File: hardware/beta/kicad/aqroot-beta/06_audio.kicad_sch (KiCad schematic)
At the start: 6 parts, among them U5 MAX98357A

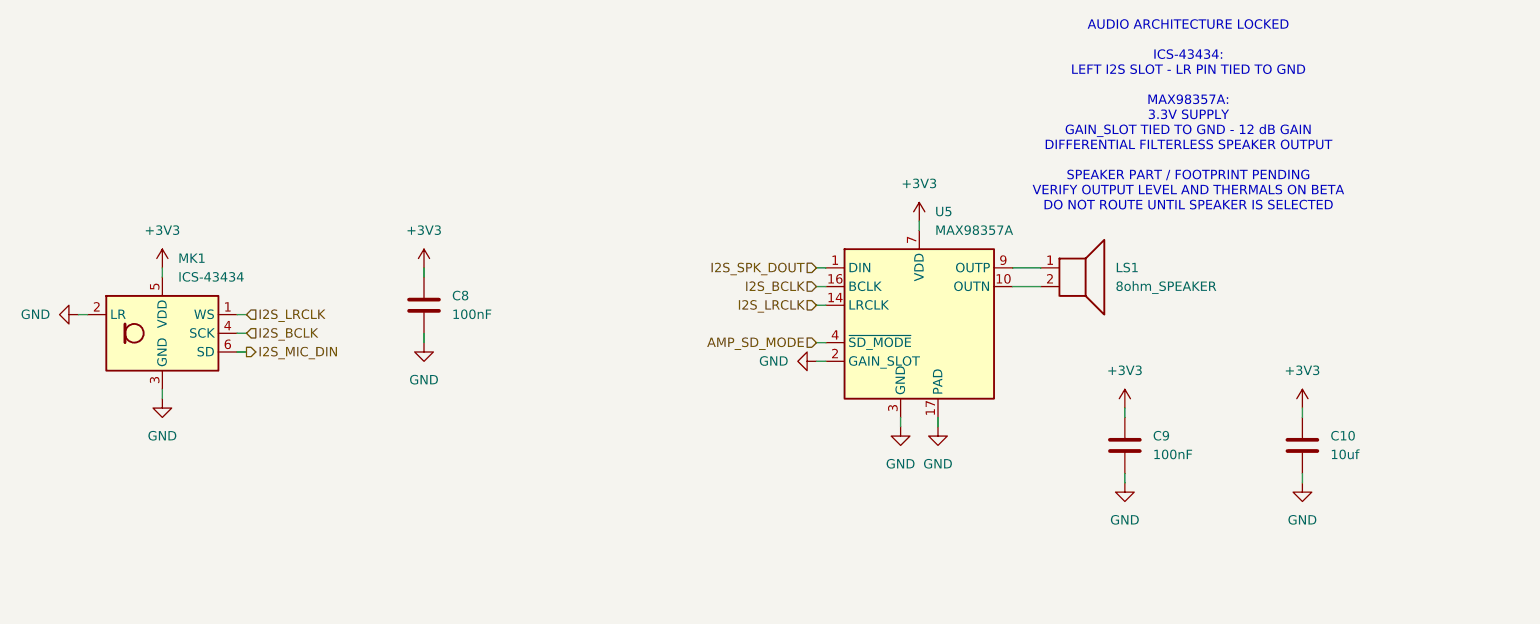
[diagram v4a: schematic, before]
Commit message: AQROOT Beta: convert speaker to off-board JST connection
Implements OPTION C, off-board wired speaker.

LS1 is reclassified OFF_BOARD. Value becomes 8R_SPEAKER_OFFBOARD, Mounting is
OFF_BOARD, and the previously locked board-mounted SKU (Same Sky CMS-1535-058SP)
is retired in favour of a class spec: 8 ohm, >=0.5 W, ~15 mm class, SKU
FINALIZES WITH ENCLOSURE. The symbol is marked exclude-from-board, so LS1 is
intentionally footprintless and drops out of the board netlist. No PCB footprint
was created for the speaker body, by design.

J6 added - JST B2B-PH-K-S, PH series, 2.00 mm pitch, board-side vertical
through-hole header, footprint
Connector_JST:JST_PH_B2B-PH-K_1x02_P2.00mm_Vertical. Verified before assignment:
2 pads, 2.00 mm pitch, through-hole, vertical, pin 1 keyed roundrect and pin 2
oval, drill 0.75, citing JST's own ePH.pdf. This is the same land pattern already
used by the J4 battery connector, so the choice is consistent with existing repo
practice. J6 is the next free connector reference; J1-J5 were not reused.

The MAX98357A path and amplifier architecture are unchanged. The differential
output pair is now named for polarity: U5 OUTP -> SPK_P -> J6 pin 1, U5 OUTN ->
SPK_N -> J6 pin 2, with LS1 shown on the same nodes as the off-board load. A
sheet note records OFF-BOARD SPEAKER / 8R >=0.5W / JST PH 2.0 mm /
ENCLOSURE-MOUNTED plus the pin-to-polarity mapping, and the stale
"DO NOT ROUTE UNTIL SPEAKER IS SELECTED" note is replaced.

Netlist delta is exactly the intended one: J6 joins SPK_P and SPK_N, U5 pins 9
and 10 move from the auto-named Net-(U5-OUTP/OUTN) to the labelled SPK_P/SPK_N,
and LS1 leaves the board netlist because it is now off-board. Net count is
unchanged at 174 - the two auto-named nets were renamed, not added. Nothing else
in the design changed. Canonical ERC holds at 58 raw / 5 errors / 53 warnings
with 58 live exclusions, 0 stale and 0 unexplained real defects.

Board-mounted missing footprints are now SW1-SW8 only.

Co-Authored-By: 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
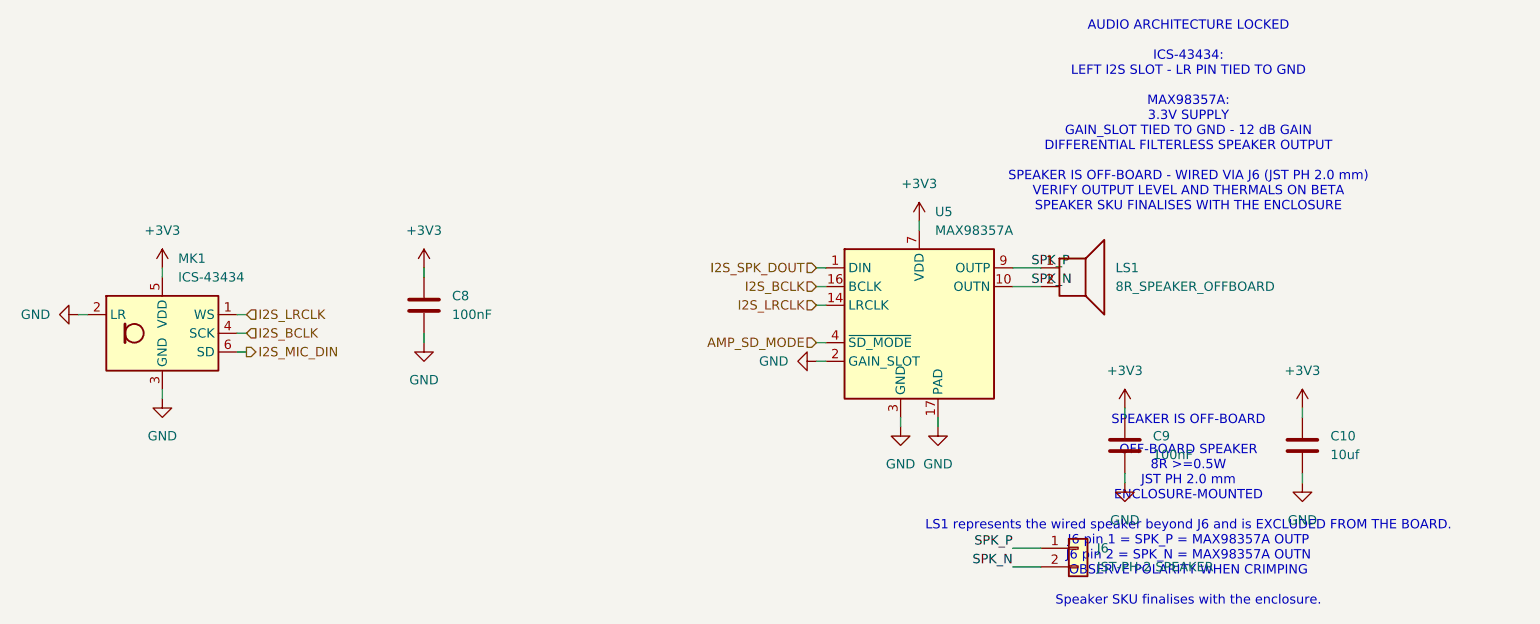
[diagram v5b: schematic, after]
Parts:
- added J6: JST-PH-2 SPEAKER, Connector_JST:JST_PH_B2B-PH-K_1x02_P2.00mm_Vertical, symbol Connector_Generic:Conn_01x02
- LS1: value 8ohm_SPEAKER -> 8R_SPEAKER_OFFBOARD; MPN CMS-1535-058SP -> SKU FINALIZES WITH ENCLOSURE; Manufacturer Same Sky (CUI Devices) -> TBD - selected with the enclosure; Mounting (none) -> OFF_BOARD; Note Audio circuit unchanged - driven differentially from MAX983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 -> OFF_BOARD / WIRED SPEAKER / 8R >=0.5W / SKU FINALIZES WITH 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; Package 15 mm round solder-pad speaker, 8 ohm - part LOCKED. Footpr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 -> OFF_BOARD WIRED SPEAKER, 8 ohm, >=0.5 W, ~15 mm class. No P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
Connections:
- net SPK_N: now reaches LS1.2, U5.10 (OUTN)
- net SPK_N: now also J6.2 (Pin_2)
- net SPK_P: now reaches LS1.1, U5.9 (OUTP)
- net SPK_P: now also J6.1 (Pin_1)
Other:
- note added: "AUDIO ARCHITECTURE LOCKED ICS-43434: LEFT I2S SLOT - LR PIN TIED TO GND MAX98357A: 3.3V SUPPLY GAIN_SLOT TIED TO GND - 12 dB GAIN DIFFERENTIAL FILTERLESS SPEAKER OUTPUT SPEAKER IS OFF-BOARD - WIRED VIA J6 (JST PH 2.0 mm) VERIFY OUTPUT LEVEL AND THERMALS ON BETA SPEAKER SKU FINALISES WITH THE ENCLOSURE"
- note added: "SPEAKER IS OFF-BOARD OFF-BOARD SPEAKER 8R >=0.5W JST PH 2.0 mm ENCLOSURE-MOUNTED LS1 represents the wired speaker beyond J6 and is EXCLUDED FROM THE BOARD. J6 pin 1 = SPK_P = MAX98357A OUTP J6 pin 2 = SPK_N = MAX98357A OUTN OBSERVE POLARITY WHEN CRIMPING Speaker SKU finalises with the enclosure."
- note removed: "AUDIO ARCHITECTURE LOCKED ICS-43434: LEFT I2S SLOT - LR PIN TIED TO GND MAX98357A: 3.3V SUPPLY GAIN_SLOT TIED TO GND - 12 dB GAIN DIFFERENTIAL FILTERLESS SPEAKER OUTPUT SPEAKER PART / FOOTPRINT PENDING VERIFY OUTPUT LEVEL AND THERMALS ON BETA DO NOT ROUTE UNTIL SPEAKER IS SELECTED"
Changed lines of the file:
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@@
 	(generator_version "10.0")
 	(paper "A4")
-	(text "AUDIO ARCHITECTURE LOCKED\n\nICS-43434:\nLEFT I2S SLOT - LR PIN TIED TO GND\n\nMAX98357A:\n3.3V SUPPLY\nGAIN_SLOT TIED TO GND - 12 dB GAIN\nDIFFERENTIAL FILTERLESS SPEAKER OUTPUT\n\nSPEAKER PART / FOOTPRINT PENDING\nVERIFY OUTPUT LEVEL AND THERMALS ON BETA\nDO NOT ROUTE UNTIL SPEAKER IS SELECTED"
+	(text "AUDIO ARCHITECTURE LOCKED\n\nICS-43434:\nLEFT I2S SLOT - LR PIN TIED TO GND\n\nMAX98357A:\n3.3V SUPPLY\nGAIN_SLOT TIED TO GND - 12 dB GAIN\nDIFFERENTIAL FILTERLESS SPEAKER OUTPUT\n\nSPEAKER IS OFF-BOARD - WIRED VIA J6 (JST PH 2.0 mm)\nVERIFY OUTPUT LEVEL AND THERMALS ON BETA\nSPEAKER SKU FINALISES WITH THE ENCLOSURE"
 		(exclude_from_sim no)
 		(at 256.286 51.816 0)
@@
 		(exclude_from_sim no)
 		(in_bom yes)
-		(on_board yes)
+		(on_board no)
 		(in_pos_files yes)
 		(dnp no)
@@
 			)
 		)
-		(property "Value" "8ohm_SPEAKER"
+		(property "Value" "8R_SPEAKER_OFFBOARD"
 			(at 246.38 74.9299 0)
 			(show_name no)
@@
 			)
 		)
-		(property "Note" "Audio circuit unchanged - driven differentially from MAX98357A OUTP/OUTN. Enclosure cavity, grille and acoustic sealing are a mechanical-phase check. Exact body height, mounting method and pad geometry NOT recorded here; take them from the Same Sky datasheet."
+		(property "Note" "OFF_BOARD / WIRED SPEAKER / 8R >=0.5W / SKU FINALIZES WITH ENCLOSURE. Implementation is OPTION C, off-board wired speaker. The MAX98357A differential output path is unchanged: U5 OUTP -> SPK_P and U5 OUTN -> SPK_N, brought to the board edge at J6 and out to the speaker on a crimped lead. LS1 is marked exclude-from-board, so it is intentionally footprintless and must NOT be counted as a missing board footprint. Target class 8 ohm, >=0.5 W, ~15 mm; exact SKU is deferred to enclosure/mechanical selection."
 			(at 241.3 72.39 0)
 			(hide yes)
@@
 			)
 		)
-		(property "Package" "15 mm round solder-pad speaker, 8 ohm - part LOCKED. Footprint BLOCKED: needs the official Same Sky mechanical drawing / land pattern."
+		(property "Package" "OFF_BOARD WIRED SPEAKER, 8 ohm, >=0.5 W, ~15 mm class. No PCB footprint by design - the speaker is enclosure-mounted and wired to the board through J6 (JST PH 2.0 mm)."
 			(at 241.3 72.39 0)
 			(hide yes)
@@
 			)
 		)
-		(property "Manufacturer" "Same Sky (CUI Devices)"
+		(property "Manufacturer" "TBD - selected with the enclosure"
 			(at 241.3 72.39 0)
 			(hide yes)
@@
 			)
 		)
-		(property "MPN" "CMS-1535-058SP"
+		(property "MPN" "SKU FINALIZES WITH ENCLOSURE"
 			(at 241.3 72.39 0)
 			(hide yes)
@@
 		)
 		(property "Description" "Speaker"
+			(at 241.3 72.39 0)
+			(hide yes)
+			(show_name no)
+			(do_not_autoplace no)
+			(effects
+				(font
+					(size 1.27 1.27)
+				)
+			)
+		)
+		(property "Mounting" "OFF_BOARD"
 			(at 241.3 72.39 0)
 			(hide yes)
@@
 			)
 		)
+	)
+	(symbol
+		(lib_id "Connector_Generic:Conn_01x02")
+		(at 241.3 110.49 0)
+		(unit 1)
+		(body_style 1)
+		(exclude_from_sim no)
+		(in_bom yes)
+		(on_board yes)
+		(in_pos_files yes)
+		(dnp no)
+		(fields_autoplaced yes)
+		(property "Reference" "J6"
+			(at 243.84 110.49 0)
+			(show_name no)
+			(do_not_autoplace no)
+			(effects
+				(font
+					(size 1.27 1.27)
+				)
+				(justify left)
+			)
+		)
+		(property "Value" "JST-PH-2 SPEAKER"
+			(at 243.84 113.03 0)
+			(show_name no)
+			(do_not_autoplace no)
+			(effects
+				(font
+					(size 1.27 1.27)
+				)
+				(justify left)
+			)
+		)
+		(property "Footprint" "Connector_JST:JST_PH_B2B-PH-K_1x02_P2.00mm_Vertical"
+			(at 241.3 110.49 0)
+			(hide yes)
+			(show_name no)
+			(do_not_autoplace no)
+			(effects
+				(font
+					(size 1.27 1.27)
+				)
+			)
+		)
+		(property "Datasheet" ""
+			(at 241.3 110.49 0)
+			(hide yes)
+			(show_name no)
+			(do_not_autoplace no)
+			(effects
+				(font
+					(size 1.27 1.27)
+				)
+			)
+		)
+		(property "Description" "Generic connector, single row, 01x02, script generated (kicad-library-utils/schlib/autogen/connector/)"
+			(at 241.3 110.49 0)
+			(hide yes)
+			(show_name no)
+			(do_not_autoplace no)
+			(effects
+				(font
+					(size 1.27 1.27)
+				)
+			)
+		)
+		(property "Manufacturer" "JST"
+			(at 241.3 110.49 0)
+			(hide yes)
+			(show_name no)
+			(do_not_autoplace no)
+			(effects
+				(font
+					(size 1.27 1.27)
+				)
+			)
+		)
+		(property "MPN" "B2B-PH-K-S"
+			(at 241.3 110.49 0)
+			(hide yes)
+			(show_name no)
+			(do_not_autoplace no)
+			(effects
+				(font
+					(size 1.27 1.27)
+				)
+			)
+		)
+		(property "Package" "JST PH series, 2 pin, 2.00 mm pitch, vertical through-hole board-side header"
+			(at 241.3 110.49 0)
+			(hide yes)
+			(show_name no)
+			(do_not_autoplace no)
+			(effects
+				(font
+					(size 1.27 1.27)
+				)
+			)
+		)
+		(property "Mounting" "BOARD_MOUNTED"
+			(at 241.3 110.49 0)
+			(hide yes)
+			(show_name no)
+			(do_not_autoplace no)
+			(effects
+				(font
+					(size 1.27 1.27)
+				)
+			)
+		)
+		(property "Note" "Board-side speaker connector. OFF-BOARD SPEAKER / 8R >=0.5W / JST PH 2.0 mm / ENCLOSURE-MOUNTED. Pin 1 = SPK_P and pin 2 = SPK_N, matching MAX98357A OUTP and OUTN; observe this polarity when crimping the speaker lead. Footprint Connector_JST:JST_PH_B2B-PH-K_1x02_P2.00mm_Vertical is the same land pattern already used for the J4 battery connector."
+			(at 241.3 110.49 0)
+			(hide yes)
+			(show_name no)
+			(do_not_autoplace no)
+			(effects
+				(font
+					(size 1.27 1.27)
+				)
+			)
+		)
+		(pin "1"
+		)
+		(pin "2"
+		)
+		(instances
+			(project "aqroot-Beta"
+				(path "/8a0ad1ee-a49e-4cff-9a78-44823e373405/74cc17f2-e3bd-4f3f-b221-e9414b1e23ac"
+					(reference "J6")
+					(unit 1)
+				)
+			)
+		)
+	)
+	(label "SPK_P"
+		(at 234.95 72.39 0)
+		(fields_autoplaced yes)
+		(effects
+			(font
+				(size 1.27 1.27)
+			)
+			(justify left bottom)
+		)
+	)
+	(label "SPK_N"
+		(at 234.95 74.93 0)
+		(fields_autoplaced yes)
+		(effects
+			(font
+				(size 1.27 1.27)
+			)
+			(justify left bottom)
+		)
+	)
+	(wire
+		(pts
+			(xy 236.22 110.49) (xy 232.41 110.49)
+		)
+		(stroke
+			(width 0)
+			(type default)
+		)
+	)
+	(wire
+		(pts
+			(xy 236.22 113.03) (xy 232.41 113.03)
+		)
+		(stroke
+			(width 0)
+			(type default)
+		)
+	)
+	(label "SPK_P"
+		(at 232.41 110.49 180)
+		(fields_autoplaced yes)
+		(effects
+			(font
+				(size 1.27 1.27)
+			)
+			(justify right bottom)
+		)
+	)
+	(label "SPK_N"
+		(at 232.41 113.03 180)
+		(fields_autoplaced yes)
+		(effects
+			(font
+				(size 1.27 1.27)
+			)
+			(justify right bottom)
+		)
+	)
+	(text "SPEAKER IS OFF-BOARD\n\nOFF-BOARD SPEAKER\n8R >=0.5W\nJST PH 2.0 mm\nENCLOSURE-MOUNTED\n\nLS1 represents the wired speaker beyond J6 and is EXCLUDED FROM THE BOARD.\nJ6 pin 1 = SPK_P = MAX98357A OUTP\nJ6 pin 2 = SPK_N = MAX98357A OUTN\nOBSERVE POLARITY WHEN CRIMPING\n\nSpeaker SKU finalises with the enclosure."
+		(exclude_from_sim no)
+		(at 256.286 105.41 0)
+		(effects
+			(font
+				(size 1.27 1.27)
+			)
+		)
